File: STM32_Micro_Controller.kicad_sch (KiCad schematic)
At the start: 1 part, among them U1 STM32F103C8T6

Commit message: Add files via upload
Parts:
- renumbered U1 to U?
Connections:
- net TIMEPULSE: now reaches U?.11 (PA1)
- net IMU_INT1: now reaches U?.18 (PB0)
- net IMU_CS: now reaches U?.19 (PB1)
- net UART_MCU_TX_GPS_RX: now reaches U?.30 (PA9)
- net UART_GPS_TX_MCU_RX: now reaches U?.31 (PA10)
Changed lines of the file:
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@@
+		)
+	)
+	(global_label "TIMEPULSE"
+		(shape input)
+		(at 148.59 62.23 0)
+		(fields_autoplaced yes)
+		(effects
+			(font
+				(size 1.27 1.27)
+			)
+			(justify left)
+		)
+		(property "Intersheetrefs" "${INTERSHEET_REFS}"
+			(at 161.7351 62.23 0)
+			(effects
+				(font
+					(size 1.27 1.27)
+				)
+				(justify left)
+				(hide yes)
+			)
+		)
+	)
+	(global_label "IMU_INT1"
+		(shape input)
+		(at 113.03 87.63 180)
+		(fields_autoplaced yes)
+		(effects
+			(font
+				(size 1.27 1.27)
+			)
+			(justify right)
+		)
+		(property "Intersheetrefs" "${INTERSHEET_REFS}"
+			(at 101.5781 87.63 0)
+			(effects
+				(font
+					(size 1.27 1.27)
+				)
+				(justify right)
+				(hide yes)
+			)
+		)
+	)
+	(global_label "UART_MCU_TX_GPS_RX"
+		(shape input)
+		(at 148.59 82.55 0)
+		(fields_autoplaced yes)
+		(effects
+			(font
+				(size 1.27 1.27)
+			)
+			(justify left)
+		)
+		(property "Intersheetrefs" "${INTERSHEET_REFS}"
+			(at 172.5603 82.55 0)
+			(effects
+				(font
+					(size 1.27 1.27)
+				)
+				(justify left)
+				(hide yes)
+			)
 		)
 	)
@@
 				)
 				(justify left)
+				(hide yes)
+			)
+		)
+	)
+	(global_label "UART_GPS_TX_MCU_RX"
+		(shape input)
+		(at 148.59 85.09 0)
+		(fields_autoplaced yes)
+		(effects
+			(font
+				(size 1.27 1.27)
+			)
+			(justify left)
+		)
+		(property "Intersheetrefs" "${INTERSHEET_REFS}"
+			(at 172.5603 85.09 0)
+			(effects
+				(font
+					(size 1.27 1.27)
+				)
+				(justify left)
+				(hide yes)
+			)
+		)
+	)
+	(global_label "IMU_CS"
+		(shape input)
+		(at 113.03 90.17 180)
+		(fields_autoplaced yes)
+		(effects
+			(font
+				(size 1.27 1.27)
+			)
+			(justify right)
+		)
+		(property "Intersheetrefs" "${INTERSHEET_REFS}"
+			(at 103.211 90.17 0)
+			(effects
+				(font
+					(size 1.27 1.27)
+				)
+				(justify right)
 				(hide yes)
 			)
@@
 		(on_board yes)
 		(dnp no)
-		(property "Reference" "U1"
+		(property "Reference" "U?"
 			(at 144.272 53.594 0)
 			(effects
@@
 		)
 		(instances
+			(project "STM32_Micro_Controller (1)"
+				(path "/21af2904-4211-4090-9120-4036a9676746"
+					(reference "U?")
+					(unit 1)
+				)
+			)
 			(project "flight-controller-basic"
 				(path "/e04fbe87-dc7c-407c-abef-b71ed1bbe06a/9ed827cc-d6ed-4e01-b191-8b39b0ab77a8"
@@
 		(dnp no)
 		(fields_autoplaced yes)
-		(property "Reference" "#PWR01"
+		(property "Reference" "#PWR?"
 			(at 130.81 142.24 0)
 			(effects
@@
 		)
 		(instances
+			(project "STM32_Micro_Controller (1)"
+				(path "/21af2904-4211-4090-9120-4036a9676746"
+					(reference "#PWR?")
+					(unit 1)
+				)
+			)
 			(project "flight-controller-basic"
 				(path "/e04fbe87-dc7c-407c-abef-b71ed1bbe06a/9ed827cc-d6ed-4e01-b191-8b39b0ab77a8"
@@
 		(on_board yes)
 		(dnp no)
-		(property "Reference" "#PWR02"
+		(property "Reference" "#PWR?"
 			(at 125.73 53.34 0)
 			(effects
@@
 		)
 		(instances
+			(project "STM32_Micro_Controller (1)"
+				(path "/21af2904-4211-4090-9120-4036a9676746"
+					(reference "#PWR?")
+					(unit 1)
+				)
+			)
 			(project "flight-controller-basic"
 				(path "/e04fbe87-dc7c-407c-abef-b71ed1bbe06a/9ed827cc-d6ed-4e01-b191-8b39b0ab77a8"
@@
 		)
 	)
+	(sheet_instances
+		(path "/"
+			(page "1")
+		)
+	)
+	(embedded_fonts no)
 )

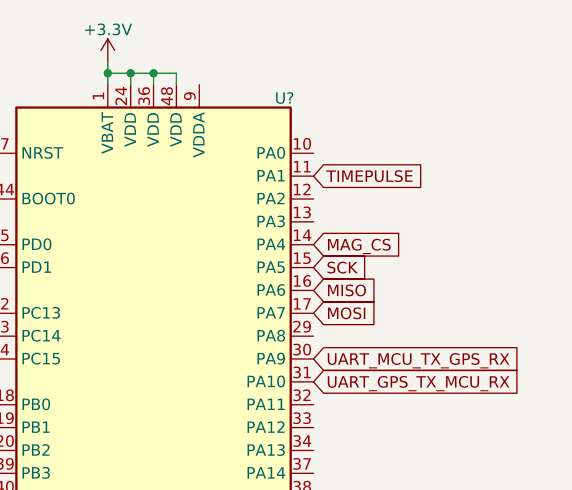
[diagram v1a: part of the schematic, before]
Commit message: Added the labels for where we will connect the Micro SD module.
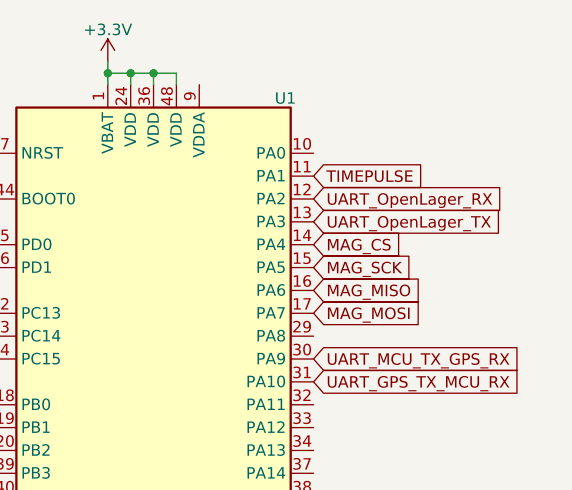
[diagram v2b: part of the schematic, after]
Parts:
- gave numbers to parts that had none: 1
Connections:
- net UART_OpenLager_RX: now reaches U1.12 (PA2)
- net UART_OpenLager_TX: now reaches U1.13 (PA3)
- net MISO renamed MAG_MISO
- net MOSI renamed MAG_MOSI
- net SCK renamed MAG_SCK
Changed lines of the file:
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@@
 		)
 	)
-	(global_label "SCK"
+	(global_label "MAG_SCK"
 		(shape input)
 		(at 148.59 72.39 0)
@@
 		)
 		(property "Intersheetrefs" "${INTERSHEET_REFS}"
-			(at 155.3247 72.39 0)
+			(at 160.1023 72.39 0)
 			(effects
 				(font
@@
 		)
 	)
+	(global_label "UART_OpenLager_RX"
+		(shape input)
+		(at 148.59 64.77 0)
+		(fields_autoplaced yes)
+		(effects
+			(font
+				(size 1.27 1.27)
+			)
+			(justify left)
+		)
+		(property "Intersheetrefs" "${INTERSHEET_REFS}"
+			(at 170.5646 64.77 0)
+			(effects
+				(font
+					(size 1.27 1.27)
+				)
+				(justify left)
+				(hide yes)
+			)
+		)
+	)
 	(global_label "IMU_INT1"
 		(shape input)
@@
 		)
 	)
-	(global_label "MISO"
+	(global_label "MAG_MISO"
 		(shape input)
 		(at 148.59 74.93 0)
@@
 		)
 		(property "Intersheetrefs" "${INTERSHEET_REFS}"
-			(at 156.1714 74.93 0)
+			(at 160.949 74.93 0)
 			(effects
 				(font
@@
 		)
 	)
-	(global_label "MOSI"
+	(global_label "UART_OpenLager_TX"
+		(shape input)
+		(at 148.59 67.31 0)
+		(fields_autoplaced yes)
+		(effects
+			(font
+				(size 1.27 1.27)
+			)
+			(justify left)
+		)
+		(property "Intersheetrefs" "${INTERSHEET_REFS}"
+			(at 170.2622 67.31 0)
+			(effects
+				(font
+					(size 1.27 1.27)
+				)
+				(justify left)
+				(hide yes)
+			)
+		)
+	)
+	(global_label "MAG_MOSI"
 		(shape input)
 		(at 148.59 77.47 0)
@@
 		)
 		(property "Intersheetrefs" "${INTERSHEET_REFS}"
-			(at 156.1714 77.47 0)
+			(at 160.949 77.47 0)
 			(effects
 				(font
@@
 		(on_board yes)
 		(dnp no)
-		(property "Reference" "U?"
+		(property "Reference" "U1"
 			(at 144.272 53.594 0)
 			(effects
@@
 		(dnp no)
 		(fields_autoplaced yes)
-		(property "Reference" "#PWR?"
+		(property "Reference" "#PWR01"
 			(at 130.81 142.24 0)
 			(effects
@@
 		(on_board yes)
 		(dnp no)
-		(property "Reference" "#PWR?"
+		(property "Reference" "#PWR02"
 			(at 125.73 53.34 0)
 			(effects
